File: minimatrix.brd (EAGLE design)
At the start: 32 x 32 mm, 9 parts

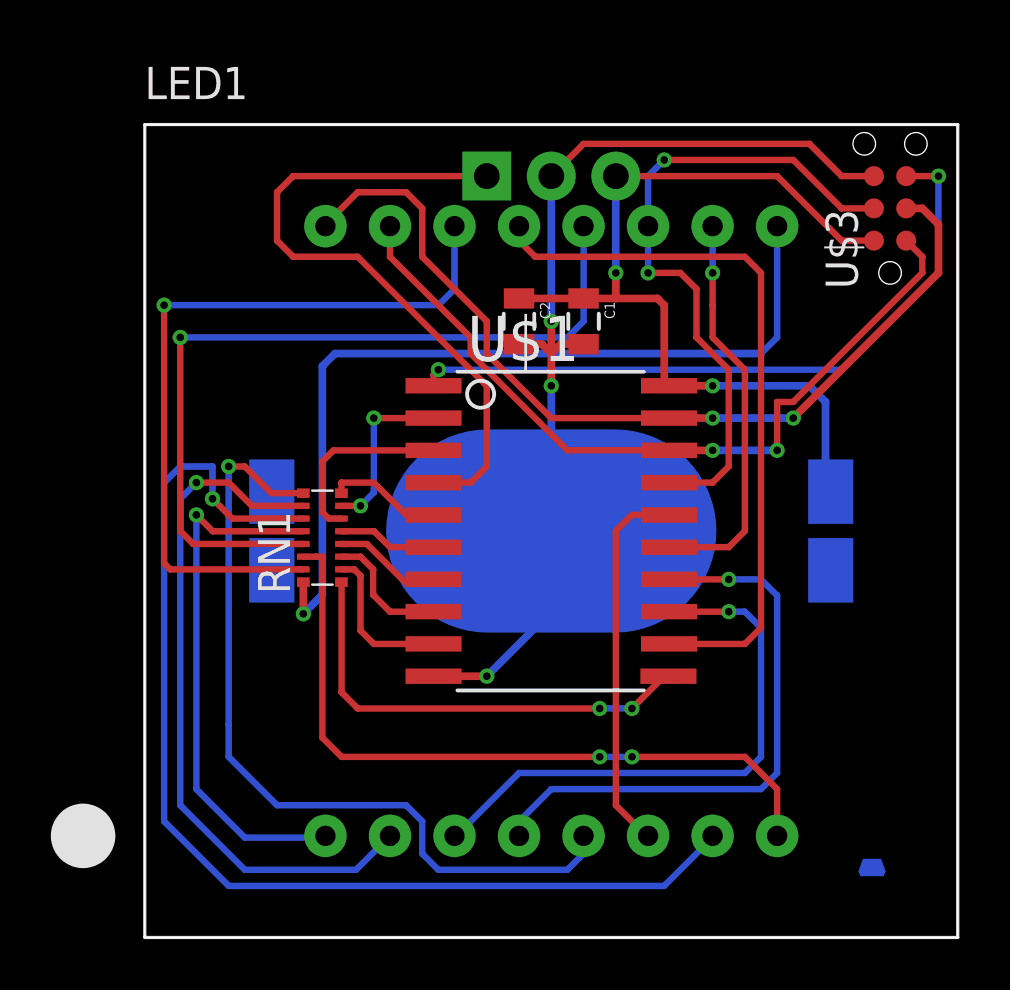
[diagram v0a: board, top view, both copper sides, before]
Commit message: Rearrange pins so the IR receiver is on an interrupt.
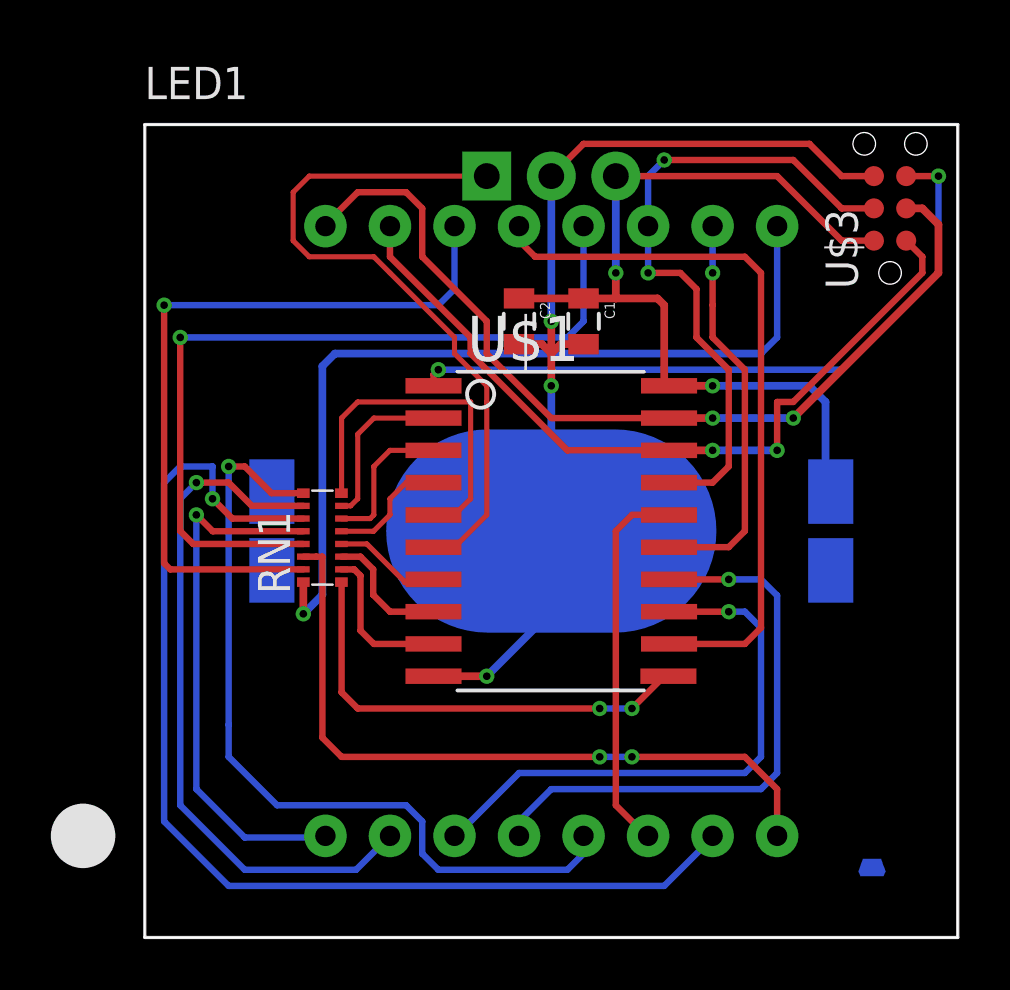
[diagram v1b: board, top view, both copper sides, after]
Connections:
- removed net N$21: U$1.4, U$2.1
- removed net R5: RN1.5, U$1.6
- new net N$1: U$1.6, U$2.1
- new net N$3: RN1.5, U$1.4
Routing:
- net N$1: track 0.00 -> 27.8 mm
- net N$21: track 26.6 -> 0.00 mm
- net R8: track 4.56 -> 13.8 mm
- net N$3: track 0.00 -> 4.79 mm
- net R5: track 3.88 -> 0.00 mm
- net R6: track 7.41 -> 5.85 mm
- net R7: track 6.77 -> 6.54 mm, vias 2 -> 0
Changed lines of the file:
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@@
 <contactref element="U$1" pad="7"/>
 <contactref element="RN1" pad="4"/>
-<wire x1="8.25" y1="16" x2="9.25" y2="16" width="0.254" layer="1"/>
-<wire x1="9.25" y1="16" x2="10.75" y2="14.5" width="0.254" layer="1"/>
+<wire x1="8.25" y1="16" x2="9.25" y2="16" width="0.2032" layer="1"/>
+<wire x1="9.25" y1="16" x2="10.75" y2="14.5" width="0.2032" layer="1"/>
 <wire x1="10.75" y1="14.5" x2="11.7695" y2="14.5" width="0.254" layer="1"/>
 <wire x1="11.7695" y1="14.5" x2="11.8745" y2="14.605" width="0.254" layer="1"/>
-</signal>
-<signal name="R5">
-<contactref element="U$1" pad="6"/>
-<contactref element="RN1" pad="5"/>
-<wire x1="8.25" y1="16.5" x2="9.535" y2="16.5" width="0.254" layer="1"/>
-<wire x1="9.535" y1="16.5" x2="10.16" y2="15.875" width="0.254" layer="1"/>
-<wire x1="10.16" y1="15.875" x2="11.8745" y2="15.875" width="0.254" layer="1"/>
 </signal>
 <signal name="R6">
 <contactref element="U$1" pad="3"/>
 <contactref element="RN1" pad="6"/>
-<wire x1="11.8745" y1="19.685" x2="7.935" y2="19.685" width="0.254" layer="1"/>
-<wire x1="7.935" y1="19.685" x2="7.5" y2="19.25" width="0.254" layer="1"/>
-<wire x1="7.5" y1="19.25" x2="7.5" y2="17.25" width="0.254" layer="1"/>
-<wire x1="7.5" y1="17.25" x2="7.75" y2="17" width="0.254" layer="1"/>
-<wire x1="7.75" y1="17" x2="8.25" y2="17" width="0.254" layer="1"/>
+<wire x1="8.25" y1="17" x2="9.38" y2="17" width="0.2032" layer="1"/>
+<wire x1="9.38" y1="17" x2="9.525" y2="17.145" width="0.2032" layer="1"/>
+<wire x1="9.525" y1="17.145" x2="9.525" y2="19.05" width="0.2032" layer="1"/>
+<wire x1="9.525" y1="19.05" x2="10.16" y2="19.685" width="0.2032" layer="1"/>
+<wire x1="10.16" y1="19.685" x2="11.8745" y2="19.685" width="0.2032" layer="1"/>
 </signal>
 <signal name="R7">
 <contactref element="U$1" pad="2"/>
 <contactref element="RN1" pad="7"/>
-<wire x1="11.8745" y1="20.955" x2="9.525" y2="20.955" width="0.254" layer="1"/>
-<via x="9.525" y="20.955" extent="1-16" drill="0.3"/>
-<wire x1="9.525" y1="20.955" x2="9.525" y2="18.025" width="0.254" layer="16"/>
-<wire x1="9.525" y1="18.025" x2="9" y2="17.5" width="0.254" layer="16"/>
-<via x="9" y="17.5" extent="1-16" drill="0.3"/>
-<wire x1="9" y1="17.5" x2="8.25" y2="17.5" width="0.254" layer="1"/>
+<wire x1="8.25" y1="17.5" x2="8.61" y2="17.5" width="0.2032" layer="1"/>
+<wire x1="8.61" y1="17.5" x2="8.89" y2="17.78" width="0.2032" layer="1"/>
+<wire x1="8.89" y1="17.78" x2="8.89" y2="20.32" width="0.2032" layer="1"/>
+<wire x1="8.89" y1="20.32" x2="9.525" y2="20.955" width="0.2032" layer="1"/>
+<wire x1="9.525" y1="20.955" x2="11.8745" y2="20.955" width="0.2032" layer="1"/>
 </signal>
 <signal name="R8">
 <contactref element="RN1" pad="8"/>
 <contactref element="U$1" pad="5"/>
-<wire x1="8.25" y1="18" x2="8.25" y2="18.41" width="0.254" layer="1"/>
-<wire x1="8.25" y1="18.41" x2="8.255" y2="18.415" width="0.254" layer="1"/>
-<wire x1="8.255" y1="18.415" x2="9.525" y2="18.415" width="0.254" layer="1"/>
-<wire x1="9.525" y1="18.415" x2="10.795" y2="17.145" width="0.254" layer="1"/>
-<wire x1="10.795" y1="17.145" x2="11.8745" y2="17.145" width="0.254" layer="1"/>
-</signal>
-<signal name="N$21">
-<contactref element="U$2" pad="1"/>
-<contactref element="U$1" pad="4"/>
-<wire x1="11.8745" y1="18.415" x2="13.335" y2="18.415" width="0.254" layer="1"/>
-<wire x1="13.335" y1="18.415" x2="13.97" y2="19.05" width="0.254" layer="1"/>
-<wire x1="13.97" y1="19.05" x2="13.97" y2="22.225" width="0.254" layer="1"/>
-<wire x1="13.97" y1="22.225" x2="8.89" y2="27.305" width="0.254" layer="1"/>
-<wire x1="8.89" y1="27.305" x2="6.35" y2="27.305" width="0.254" layer="1"/>
-<wire x1="6.35" y1="27.305" x2="5.715" y2="27.94" width="0.254" layer="1"/>
-<wire x1="5.715" y1="27.94" x2="5.715" y2="29.845" width="0.254" layer="1"/>
-<wire x1="5.715" y1="29.845" x2="6.35" y2="30.48" width="0.254" layer="1"/>
-<wire x1="6.35" y1="30.48" x2="13.97" y2="30.48" width="0.254" layer="1"/>
+<wire x1="11.8745" y1="17.145" x2="12.7" y2="17.145" width="0.2032" layer="1"/>
+<wire x1="12.7" y1="17.145" x2="13.335" y2="17.78" width="0.2032" layer="1"/>
+<wire x1="13.335" y1="17.78" x2="13.335" y2="20.32" width="0.2032" layer="1"/>
+<wire x1="13.335" y1="20.32" x2="13.335" y2="21.59" width="0.2032" layer="1"/>
+<wire x1="13.335" y1="21.59" x2="8.89" y2="21.59" width="0.2032" layer="1"/>
+<wire x1="8.89" y1="21.59" x2="8.255" y2="20.955" width="0.2032" layer="1"/>
+<wire x1="8.255" y1="20.955" x2="8.255" y2="18.005" width="0.2032" layer="1"/>
+<wire x1="8.255" y1="18.005" x2="8.25" y2="18" width="0.2032" layer="1"/>
 </signal>
 <signal name="C1">
@@
 <wire x1="19.685" y1="17.145" x2="21.1455" y2="17.145" width="0.254" layer="1"/>
 </signal>
+<signal name="N$1">
+<contactref element="U$2" pad="1"/>
+<contactref element="U$1" pad="6"/>
+<wire x1="11.8745" y1="15.875" x2="12.7" y2="15.875" width="0.2032" layer="1"/>
+<wire x1="12.7" y1="15.875" x2="13.97" y2="17.145" width="0.2032" layer="1"/>
+<wire x1="13.97" y1="17.145" x2="13.97" y2="21.59" width="0.2032" layer="1"/>
+<wire x1="10.16" y1="26.67" x2="9.525" y2="27.305" width="0.2032" layer="1"/>
+<wire x1="9.525" y1="27.305" x2="6.985" y2="27.305" width="0.2032" layer="1"/>
+<wire x1="6.985" y1="27.305" x2="6.35" y2="27.94" width="0.2032" layer="1"/>
+<wire x1="6.35" y1="27.94" x2="6.35" y2="29.845" width="0.2032" layer="1"/>
+<wire x1="6.35" y1="29.845" x2="6.985" y2="30.48" width="0.2032" layer="1"/>
+<wire x1="6.985" y1="30.48" x2="13.97" y2="30.48" width="0.2032" layer="1"/>
+<wire x1="10.16" y1="26.67" x2="12.7" y2="24.13" width="0.2032" layer="1"/>
+<wire x1="12.7" y1="24.13" x2="12.7" y2="23.495" width="0.2032" layer="1"/>
+<wire x1="12.7" y1="23.495" x2="13.97" y2="22.225" width="0.2032" layer="1"/>
+<wire x1="13.97" y1="22.225" x2="13.97" y2="21.59" width="0.2032" layer="1"/>
+</signal>
+<signal name="N$3">
+<contactref element="RN1" pad="5"/>
+<contactref element="U$1" pad="4"/>
+<wire x1="8.25" y1="16.5" x2="9.515" y2="16.5" width="0.2032" layer="1"/>
+<wire x1="9.515" y1="16.5" x2="10.16" y2="17.145" width="0.2032" layer="1"/>
+<wire x1="10.16" y1="17.145" x2="10.16" y2="17.78" width="0.2032" layer="1"/>
+<wire x1="10.16" y1="17.78" x2="10.795" y2="18.415" width="0.2032" layer="1"/>
+<wire x1="10.795" y1="18.415" x2="11.8745" y2="18.415" width="0.2032" layer="1"/>
+</signal>
 </signals>

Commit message: Rewire with fixed pinouts and better connection for IR receiver.
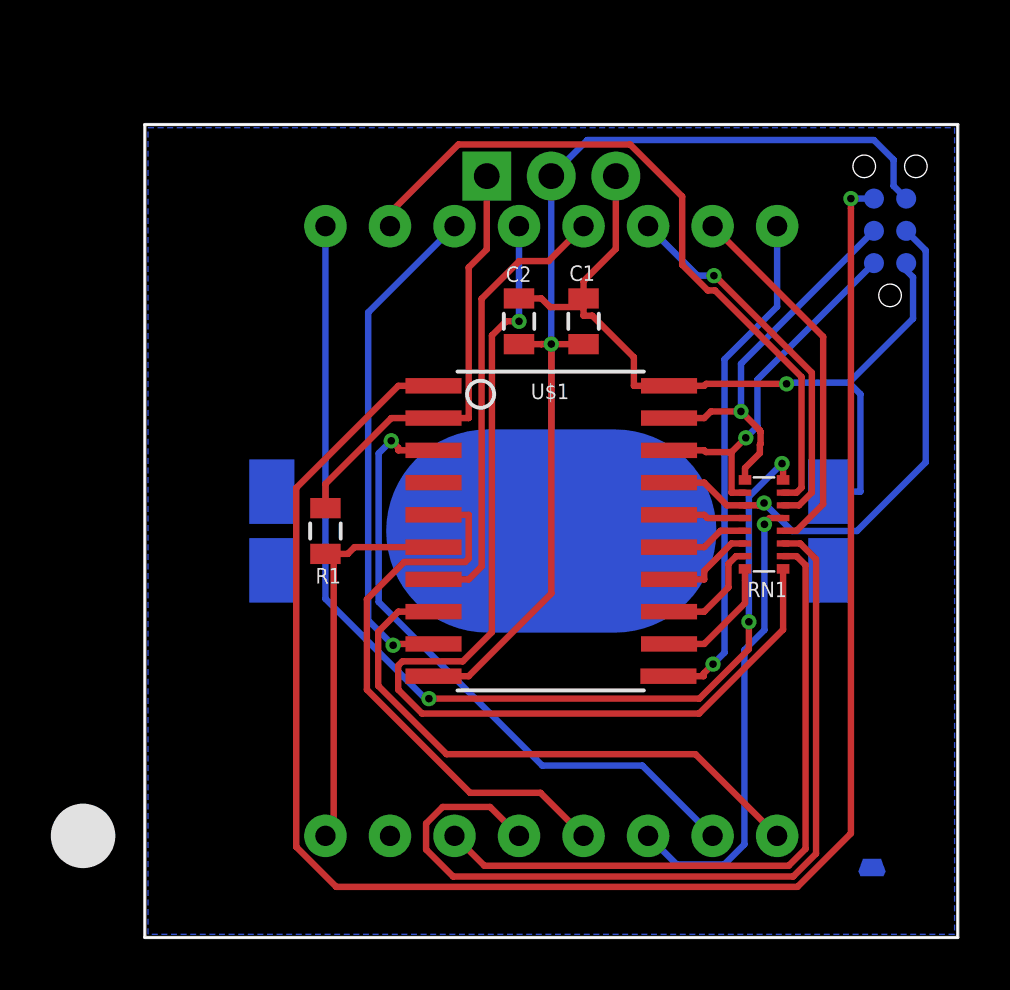
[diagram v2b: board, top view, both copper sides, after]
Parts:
- added R1: 10k, SparkFun-Passives:0805
- moved RN1 17.4 mm to (24.9, 16.8), turned to 270 degrees
- moved U$3 0.89 mm to (29.8, 25.8), flipped to the bottom
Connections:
- removed net R1: RN1.1, U$1.11
- removed net ROW2: LED1.14, RN1.15
- removed net ROW3: LED1.8, RN1.14
- removed net ROW4: LED1.12, RN1.13
- removed net ROW6: LED1.7, RN1.11
- removed net ROW7: LED1.2, RN1.10
- removed net ROW8: LED1.5, RN1.9
- new net N$10: LED1.13, RN1.9
- new net N$11: LED1.1, R1.2, U$1.6
- new net N$4: LED1.4, RN1.11
- new net N$5: LED1.10, RN1.12
- new net N$6: LED1.6, RN1.13
- new net N$7: LED1.11, RN1.14
- new net N$8: LED1.15, RN1.15
- new net N$9: LED1.16, RN1.16
- net C1: now also RN1.8; no longer LED1.13
- net C2: now also RN1.7; no longer LED1.3
- net C3: now also RN1.6; no longer LED1.4
- net C4: now also RN1.5; no longer LED1.10
- net C5: now also RN1.4; no longer LED1.6
- net C6: now also RN1.3; no longer LED1.11
- net C7: now also RN1.2; no longer LED1.15
- net C8: now also RN1.1; no longer LED1.16
- net N$1: now also R1.1, U$1.2; no longer U$1.6
- net N$3: now also LED1.3, RN1.10; no longer RN1.5, U$1.4
- net R2: now also LED1.14; no longer RN1.2
- net R3: now also LED1.8; no longer RN1.3
- net R4: now also LED1.12; no longer RN1.4
- net R6: now also LED1.7; no longer RN1.6
- net R7: now also LED1.2; no longer RN1.7, U$1.2
- net R8: now also LED1.5; no longer RN1.8
- net ROW1: now also U$1.11; no longer RN1.16
- net ROW5: now also U$1.4; no longer LED1.1, RN1.12
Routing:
- net ROW6: track 44.2 -> 0.00 mm, vias 1 -> 0
- net N$2: track 27.1 -> 70.4 mm, vias 2 -> 1
- net N$9: track 0.00 -> 42.3 mm, vias 0 -> 3
- net N$10: track 0.00 -> 41.2 mm, vias 0 -> 1
- net N$4: track 0.00 -> 34.7 mm
- net ROW4: track 32.6 -> 0.00 mm, vias 1 -> 0
- net ROW8: track 32.3 -> 0.00 mm, vias 1 -> 0
- net ROW2: track 29.9 -> 0.00 mm, vias 1 -> 0
- net ROW3: track 28.5 -> 0.00 mm, vias 2 -> 0
- net N$8: track 0.00 -> 28.4 mm
- net ROW7: track 27.4 -> 0.00 mm, vias 1 -> 0
- net C1: track 28.5 -> 5.00 mm
- net N$3: track 4.79 -> 26.8 mm
- net ROW5: track 21.2 -> 0.00 mm, vias 1 -> 0
- net C8: track 36.1 -> 15.5 mm, vias 2 -> 1
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- removed copper zone on layer 1, net GND
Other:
- board text added: "Minimatrix by Arachnid Labs"
- board text added: "www.arachnidlabs.com/minimatrix/"
